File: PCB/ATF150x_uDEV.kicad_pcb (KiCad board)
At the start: 2 copper layers, 50.8 x 20.3 mm, 22 parts, among them J1 Conn_02x05_Odd_Even, J2 VERT, J3 VERT, U1 ATF150xASx-xAx44

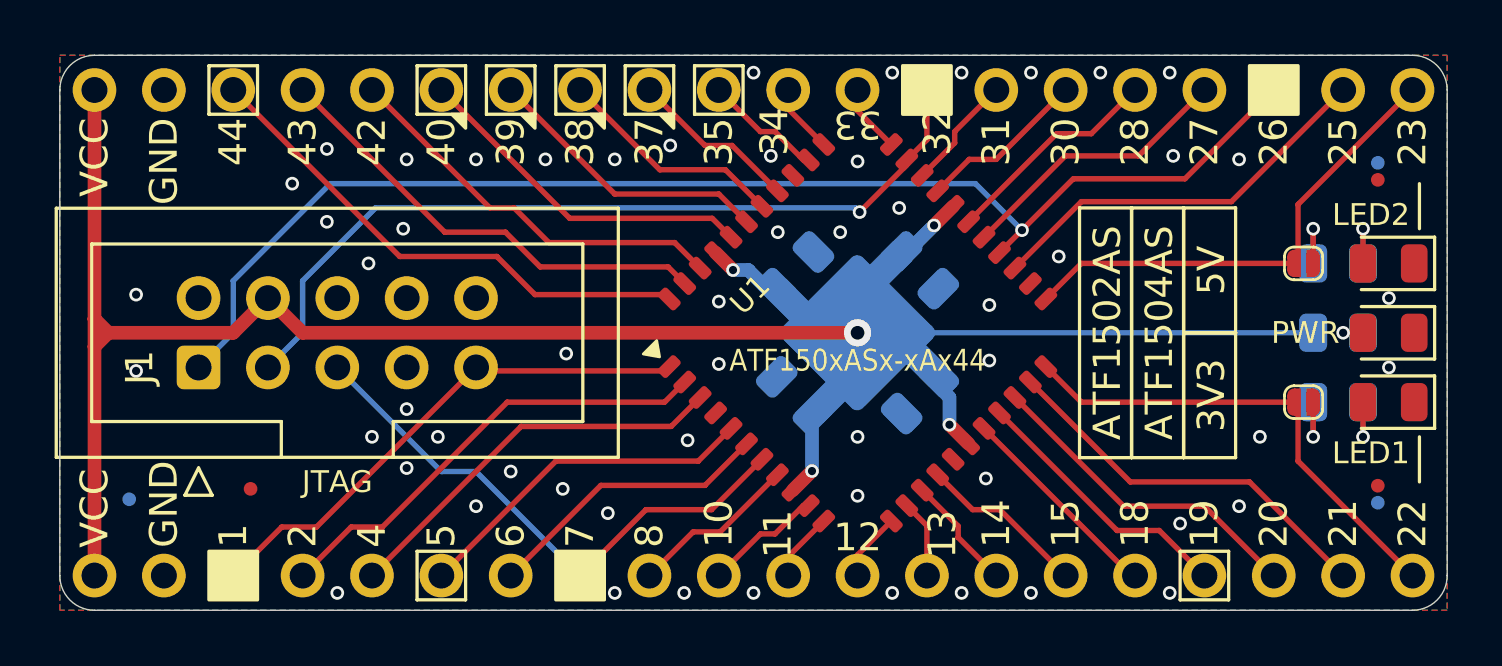
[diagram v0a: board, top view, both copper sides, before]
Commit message: fix silkscreen pin 6, remove AS from name & part number
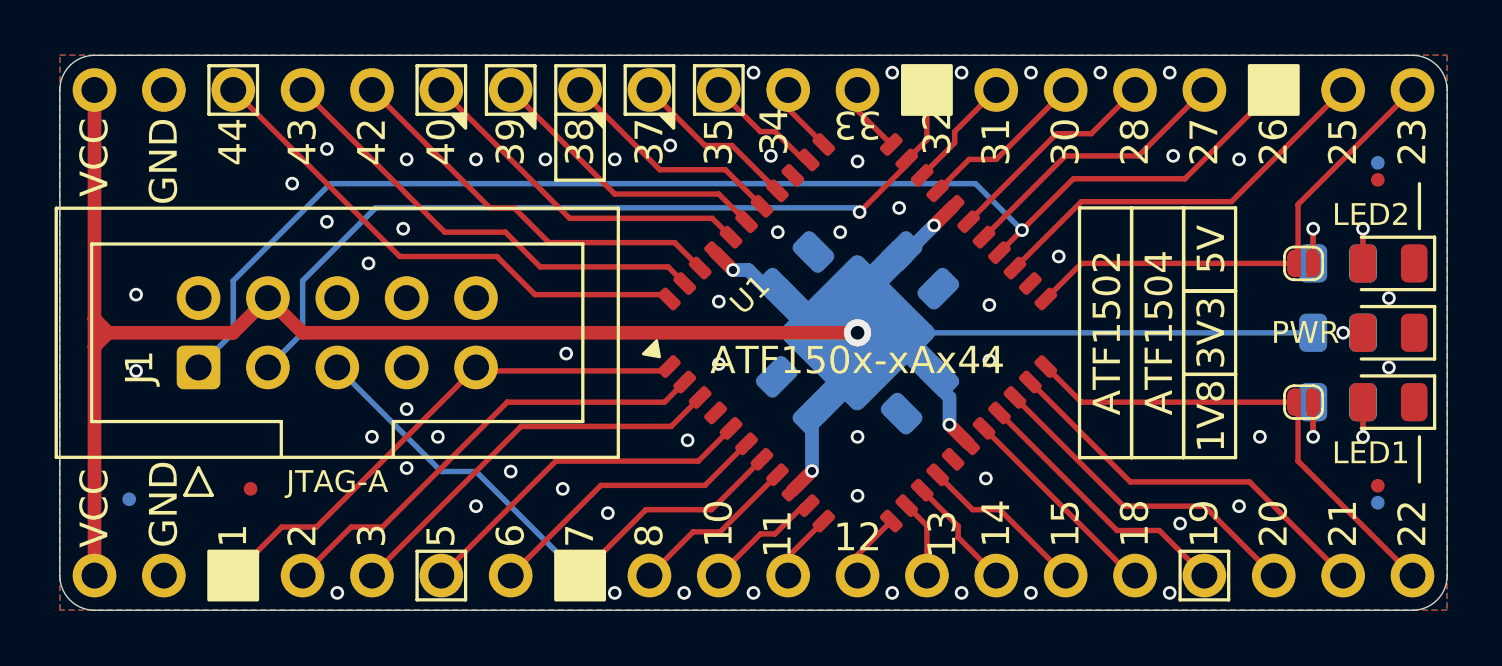
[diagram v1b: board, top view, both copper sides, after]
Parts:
- U1: value ATF150xASx-xAx44 -> ATF150x-xAx44
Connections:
- net /A8 renamed /6
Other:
- board text added: "1V8"
- board text added: "3"
- board text added: "ATF1502"
- board text added: "ATF1504"
- board text added: "JTAG-A"
- board text removed: "4"
- board text removed: "ATF1502AS"
- board text removed: "ATF1504AS"
- board text removed: "JTAG"

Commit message: add VPP to JTAG
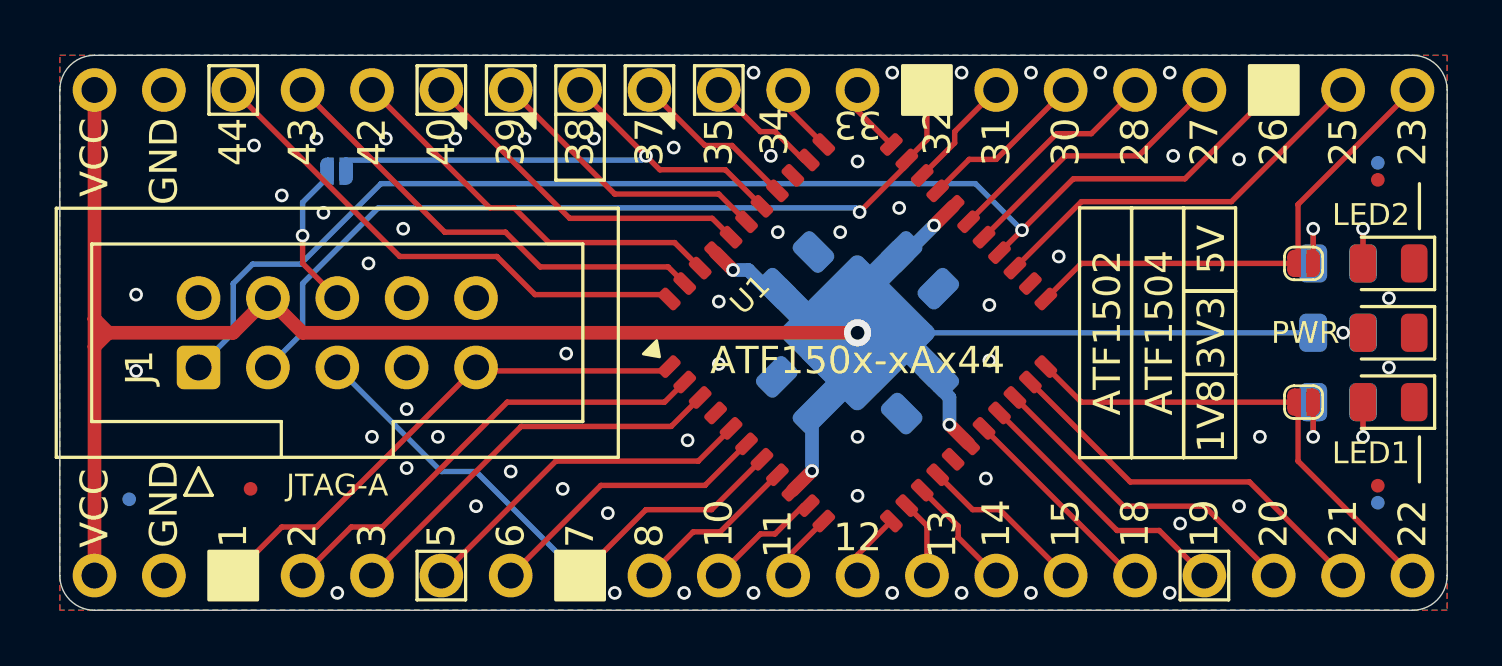
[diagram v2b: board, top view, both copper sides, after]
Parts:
- added JP3: DNP, 000_LOCAL:SolderJumper_1mm_2p_open, B.Cu at (125.7, 94.4)
- J1: value Conn_02x05_Odd_Even -> Altera JTAG-A+VPP
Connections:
- J1 pad 6: unconnected-(J1-Pin_6-Pad6) -> Net-(J1-VPP)
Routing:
- net /38/OE1/Vpp: track 8.42 -> 19.9 mm, vias 0 -> 1
- net Net-(J1-VPP): track 0.00 -> 5.57 mm, vias 0 -> 1
- net GND: vias 56 -> 57
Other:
- board text added: "${TITLE}"
- board text added: "OE1 VPP"
- board text added: "VPP"
- board text added: "v${REVISION}"
- board text removed: "${TITLE} ${REVISION}"
- board text removed: "OE1 Vpp"
